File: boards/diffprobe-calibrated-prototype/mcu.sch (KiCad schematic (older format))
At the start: 18 parts, among them J1 XILINX_JTAG, J7 CONN_01X04, U10 PIC32MM0032GPL028

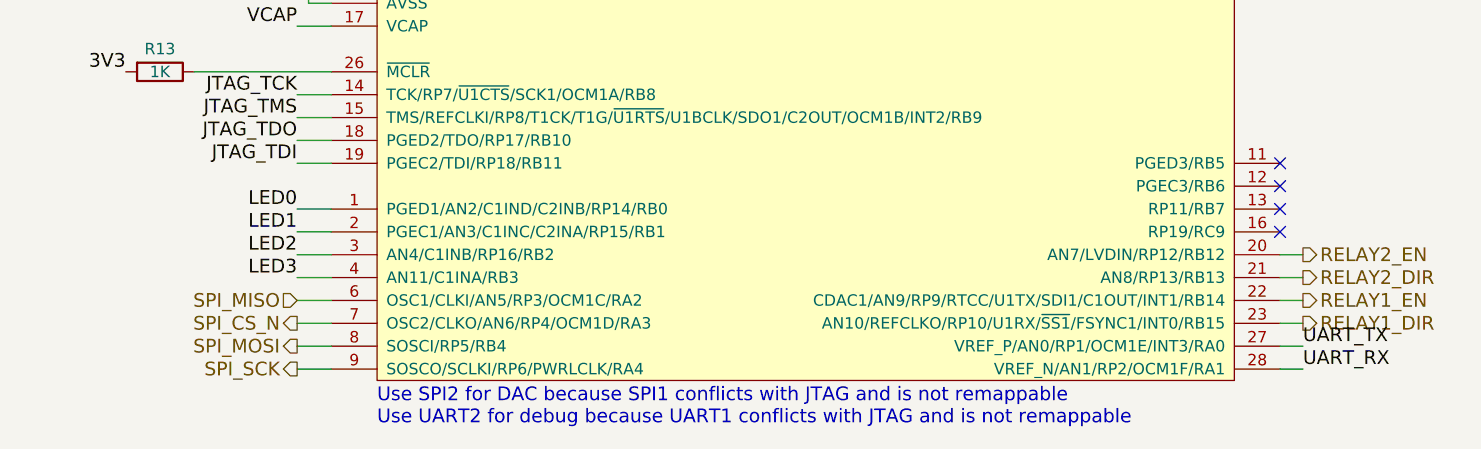
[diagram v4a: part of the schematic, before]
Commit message: Updating file: diffprobe-calibrated-prototype.kicad_pcb with current fully routed design
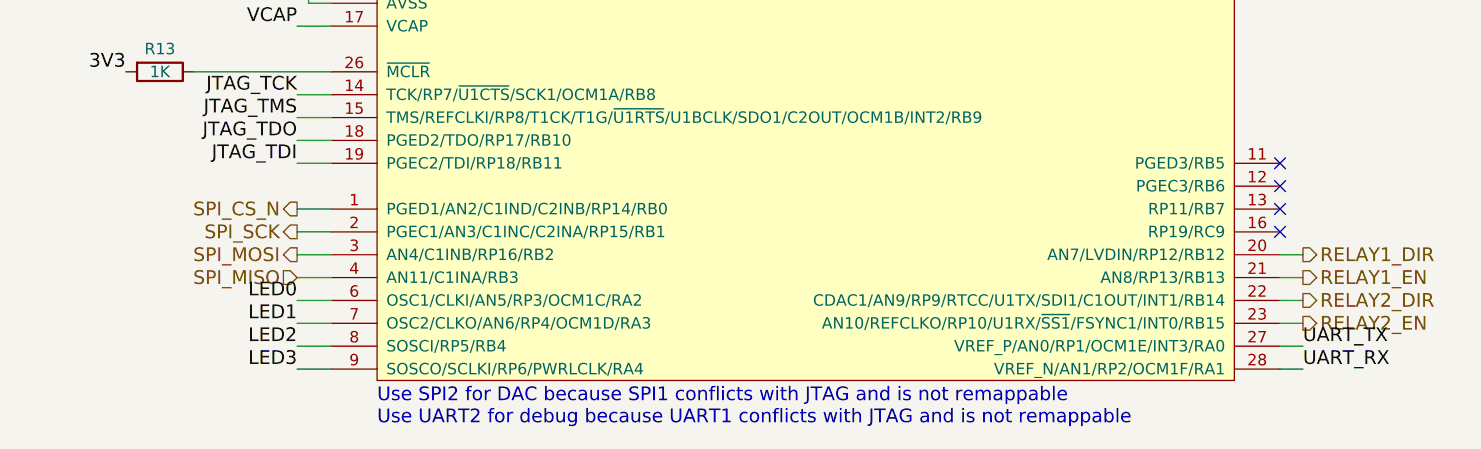
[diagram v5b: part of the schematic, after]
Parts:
- D2, D3, D4, D5: footprint azonenberg_pcb:EIA_0402_LED -> azonenberg_pcb:EIA_0603_LED
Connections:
- net LED0: now also U10.6 (OSC1/CLKI/AN5/RP3/OCM1C/RA2); no longer U10.1 (PGED1/AN2/C1IND/C2INB/RP14/RB0)
- net LED1: now also U10.7 (OSC2/CLKO/AN6/RP4/OCM1D/RA3); no longer U10.2 (PGEC1/AN3/C1INC/C2INA/RP15/RB1)
- net LED2: now also U10.8 (SOSCI/RP5/RB4); no longer U10.3 (AN4/C1INB/RP16/RB2)
- net LED3: now also U10.9 (SOSCO/SCLKI/RP6/PWRLCLK/RA4); no longer U10.4 (AN11/C1INA/RB3)
- net RELAY1_DIR: now also U10.20 (AN7/LVDIN/RP12/RB12); no longer U10.23 (AN10/REFCLKO/RP10/U1RX/~SS1~/FSYNC1/INT0/RB15)
- net RELAY1_EN: now also U10.21 (AN8/RP13/RB13); no longer U10.22 (CDAC1/AN9/RP9/RTCC/U1TX/SDI1/C1OUT/INT1/RB14)
- net RELAY2_DIR: now also U10.22 (CDAC1/AN9/RP9/RTCC/U1TX/SDI1/C1OUT/INT1/RB14); no longer U10.21 (AN8/RP13/RB13)
- net RELAY2_EN: now also U10.23 (AN10/REFCLKO/RP10/U1RX/~SS1~/FSYNC1/INT0/RB15); no longer U10.20 (AN7/LVDIN/RP12/RB12)
- net SPI_CS_N: now also U10.1 (PGED1/AN2/C1IND/C2INB/RP14/RB0); no longer U10.7 (OSC2/CLKO/AN6/RP4/OCM1D/RA3)
- net SPI_MISO: now also U10.4 (AN11/C1INA/RB3); no longer U10.6 (OSC1/CLKI/AN5/RP3/OCM1C/RA2)
- net SPI_MOSI: now also U10.3 (AN4/C1INB/RP16/RB2); no longer U10.8 (SOSCI/RP5/RB4)
- net SPI_SCK: now also U10.2 (PGEC1/AN3/C1INC/C2INA/RP15/RB1); no longer U10.9 (SOSCO/SCLKI/RP6/PWRLCLK/RA4)
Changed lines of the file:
@@
 Sheet 4 4
 Title "500 MHz Active Differential Probe"
-Date "2017-12-20"
+Date "2017-12-21"
 Rev "0.2"
 Comp "Andrew D. Zonenberg"
@@
 Wire Wire Line
 	3800 3800 3950 3800
-Text HLabel 3800 5100 0    60   Output ~ 0
+Text HLabel 3800 4600 0    60   Output ~ 0
 SPI_CS_N
-Text HLabel 3800 5200 0    60   Output ~ 0
+Text HLabel 3800 4800 0    60   Output ~ 0
 SPI_MOSI
-Text HLabel 3800 5300 0    60   Output ~ 0
+Text HLabel 3800 4700 0    60   Output ~ 0
 SPI_SCK
-Text HLabel 3800 5000 0    60   Input ~ 0
+Text HLabel 3800 4900 0    60   Input ~ 0
 SPI_MISO
 Text Notes 4150 5550 0    60   ~ 0
 Use SPI2 for DAC because SPI1 conflicts with JTAG and is not remappable\nUse UART2 for debug because UART1 conflicts with JTAG and is not remappable
 Wire Wire Line
-	3800 5000 3950 5000
-Wire Wire Line
-	3950 5100 3800 5100
-Wire Wire Line
-	3800 5200 3950 5200
-Wire Wire Line
-	3950 5300 3800 5300
+	3800 4600 3950 4600
+Wire Wire Line
+	3950 4700 3800 4700
+Wire Wire Line
+	3800 4800 3950 4800
+Wire Wire Line
+	3950 4900 3800 4900
 Text Label 1050 1050 2    60   ~ 0
 GND
@@
 Wire Wire Line
 	8200 5300 8100 5300
+Text HLabel 8200 4800 2    60   Output ~ 0
+RELAY1_DIR
+Text HLabel 8200 4900 2    60   Output ~ 0
+RELAY1_EN
+Text HLabel 8200 5000 2    60   Output ~ 0
+RELAY2_DIR
 Text HLabel 8200 5100 2    60   Output ~ 0
-RELAY1_DIR
-Text HLabel 8200 5000 2    60   Output ~ 0
-RELAY1_EN
-Text HLabel 8200 4900 2    60   Output ~ 0
-RELAY2_DIR
-Text HLabel 8200 4800 2    60   Output ~ 0
 RELAY2_EN
 Wire Wire Line
@@
 F 0 "D2" V 6188 1932 50  0000 R CNN
 F 1 "GREEN" V 6097 1932 50  0000 R CNN
-F 2 "azonenberg_pcb:EIA_0402_LED" H 6150 2050 50  0001 C CNN
+F 2 "azonenberg_pcb:EIA_0603_LED" H 6150 2050 50  0001 C CNN
 F 3 "" H 6150 2050 50  0000 C CNN
 	1    6150 2050
@@
 F 0 "D3" V 6838 1932 50  0000 R CNN
 F 1 "GREEN" V 6747 1932 50  0000 R CNN
-F 2 "azonenberg_pcb:EIA_0402_LED" H 6800 2050 50  0001 C CNN
+F 2 "azonenberg_pcb:EIA_0603_LED" H 6800 2050 50  0001 C CNN
 F 3 "" H 6800 2050 50  0000 C CNN
 	1    6800 2050
@@
 F 0 "D4" V 7438 1932 50  0000 R CNN
 F 1 "GREEN" V 7347 1932 50  0000 R CNN
-F 2 "azonenberg_pcb:EIA_0402_LED" H 7400 2050 50  0001 C CNN
+F 2 "azonenberg_pcb:EIA_0603_LED" H 7400 2050 50  0001 C CNN
 F 3 "" H 7400 2050 50  0000 C CNN
 	1    7400 2050
@@
 F 0 "D5" V 8038 1932 50  0000 R CNN
 F 1 "GREEN" V 7947 1932 50  0000 R CNN
-F 2 "azonenberg_pcb:EIA_0402_LED" H 8000 2050 50  0001 C CNN
+F 2 "azonenberg_pcb:EIA_0603_LED" H 8000 2050 50  0001 C CNN
 F 3 "" H 8000 2050 50  0000 C CNN
 	1    8000 2050
@@
 Connection ~ 6800 2200
 Connection ~ 6150 2200
-Text Label 3800 4600 2    60   ~ 0
+Text Label 3800 5000 2    60   ~ 0
 LED0
-Text Label 3800 4700 2    60   ~ 0
+Text Label 3800 5100 2    60   ~ 0
 LED1
-Text Label 3800 4800 2    60   ~ 0
+Text Label 3800 5200 2    60   ~ 0
 LED2
-Text Label 3800 4900 2    60   ~ 0
+Text Label 3800 5300 2    60   ~ 0
 LED3
 Wire Wire Line
-	3800 4900 3950 4900
-Wire Wire Line
-	3950 4800 3800 4800
-Wire Wire Line
-	3800 4700 3950 4700
-Wire Wire Line
-	3950 4600 3800 4600
+	3800 5300 3950 5300
+Wire Wire Line
+	3950 5200 3800 5200
+Wire Wire Line
+	3800 5100 3950 5100
+Wire Wire Line
+	3950 5000 3800 5000
 NoConn ~ 8100 4700
 NoConn ~ 8100 4600

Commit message: Moved a bunch of old files out of the way, added some notes that never got committed
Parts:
- C37, C38, C39, C40, C41, C42: symbol C -> device:C
- D2, D3, D4, D5: symbol LED -> device:LED
- J1: symbol XILINX_JTAG -> xilinx-azonenberg:XILINX_JTAG
- J7: symbol CONN_01X04 -> diffprobe-calibrated-prototype-rescue:CONN_01X04
- R13, R14, R15, R16, R17: symbol R -> device:R
- U10: symbol PIC32MMxGPL028 -> microchip-azonenberg:PIC32MMxGPL028
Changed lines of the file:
@@
-EESchema Schematic File Version 3
-LIBS:analog-azonenberg
-LIBS:cmos
-LIBS:cypress-azonenberg
-LIBS:hirose-azonenberg
-LIBS:memory-azonenberg
-LIBS:microchip-azonenberg
-LIBS:osc-azonenberg
-LIBS:passive-azonenberg
-LIBS:power-azonenberg
-LIBS:silego-azonenberg
-LIBS:special-azonenberg
-LIBS:xilinx-azonenberg
-LIBS:conn
-LIBS:device
+EESchema Schematic File Version 4
 LIBS:diffprobe-calibrated-prototype-cache
-EELAYER 26 0
+EELAYER 29 0
 EELAYER END
 $Descr USLetter 11000 8500
@@
 $EndDescr
 $Comp
-L CONN_01X04 J7
+L diffprobe-calibrated-prototype-rescue:CONN_01X04 J7
 U 1 1 5A1F8A2F
 P 1400 1100
@@
 	1050 1250 1200 1250
 $Comp
-L XILINX_JTAG J1
+L xilinx-azonenberg:XILINX_JTAG J1
 U 1 1 5A1F8B4D
 P 1250 2800
@@
 NoConn ~ 1250 2800
 $Comp
-L PIC32MMxGPL028 U10
+L microchip-azonenberg:PIC32MMxGPL028 U10
 U 1 1 5A2E3505
 P 4150 5350
@@
 	8100 4900 8200 4900
 $Comp
-L R R13
+L device:R R13
 U 1 1 5A386F8B
 P 3200 4000
@@
 3V3
 $Comp
-L R R14
+L device:R R14
 U 1 1 5A3872CE
 P 6150 1650
@@
 $EndComp
 $Comp
-L LED D2
+L device:LED D2
 U 1 1 5A387391
 P 6150 2050
@@
 	6000 2200 8000 2200
 $Comp
-L R R15
+L device:R R15
 U 1 1 5A3875D8
 P 6800 1650
@@
 $EndComp
 $Comp
-L LED D3
+L device:LED D3
 U 1 1 5A3875DE
 P 6800 2050
@@
 	6650 1500 6800 1500
 $Comp
-L R R16
+L device:R R16
 U 1 1 5A387669
 P 7400 1650
@@
 $EndComp
 $Comp
-L LED D4
+L device:LED D4
 U 1 1 5A38766F
 P 7400 2050
@@
 	7250 1500 7400 1500
 $Comp
-L R R17
+L device:R R17
 U 1 1 5A3876F8
 P 8000 1650
@@
 $EndComp
 $Comp
-L LED D5
+L device:LED D5
 U 1 1 5A3876FE
 P 8000 2050
@@
 NoConn ~ 8100 4400
 $Comp
-L C C37
+L device:C C37
 U 1 1 5A38C6FE
 P 950 3500
@@
 $EndComp
 $Comp
-L C C39
+L device:C C39
 U 1 1 5A38C7B6
 P 1500 3500
@@
 $EndComp
 $Comp
-L C C42
+L device:C C42
 U 1 1 5A38C81E
 P 2100 3500
@@
 Connection ~ 1500 3650
 $Comp
-L C C38
+L device:C C38
 U 1 1 5A38CB75
 P 950 4000
@@
 $EndComp
 $Comp
-L C C40
+L device:C C40
 U 1 1 5A38CBB9
 P 1500 4000
@@
 Connection ~ 950  3850
 $Comp
-L C C41
+L device:C C41
 U 1 1 5A38CDE8
 P 2050 4000
